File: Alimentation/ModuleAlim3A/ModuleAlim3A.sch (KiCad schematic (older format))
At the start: 18 parts, among them J1 Conn_01x05, J2 Conn_01x02, J3 OUTPUT, U1 PTN78060W_EUW-7, U2 ACS712xLCTR-20A

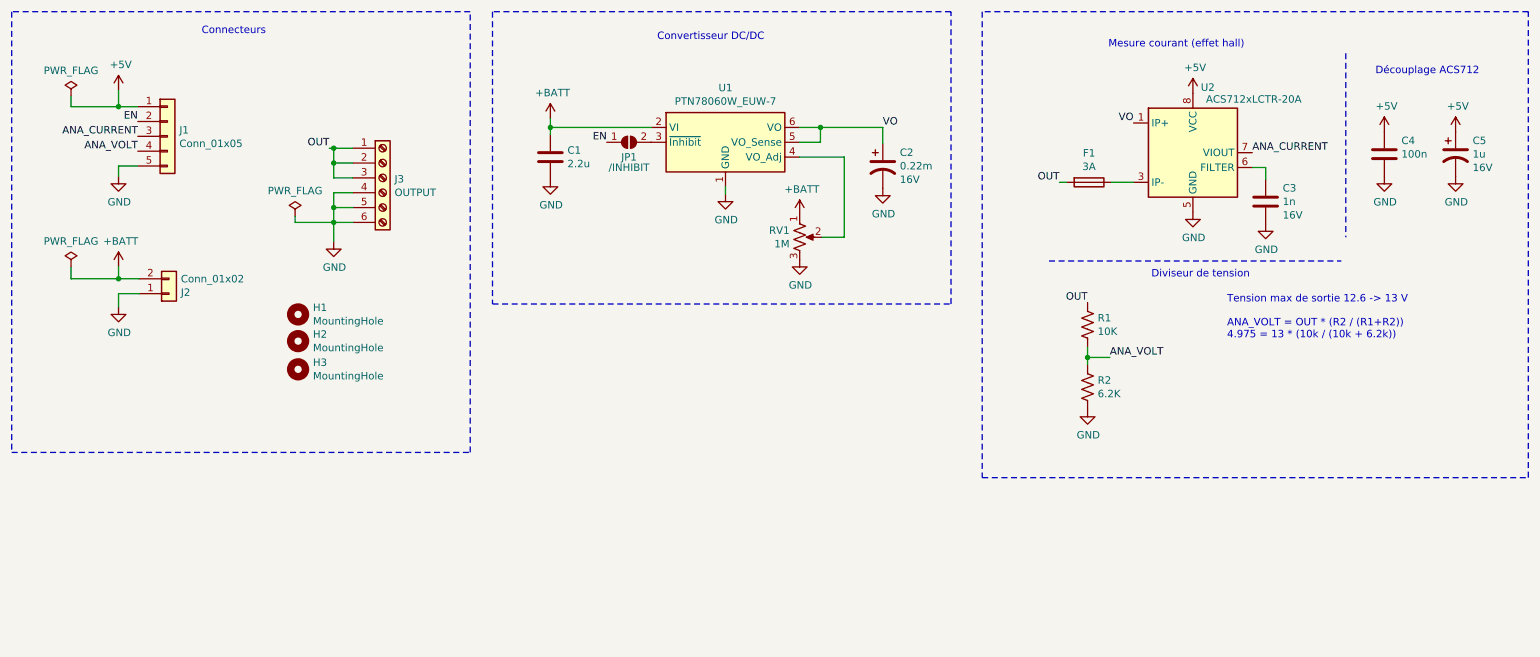
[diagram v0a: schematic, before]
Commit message: Module alim ISO, clean master alim
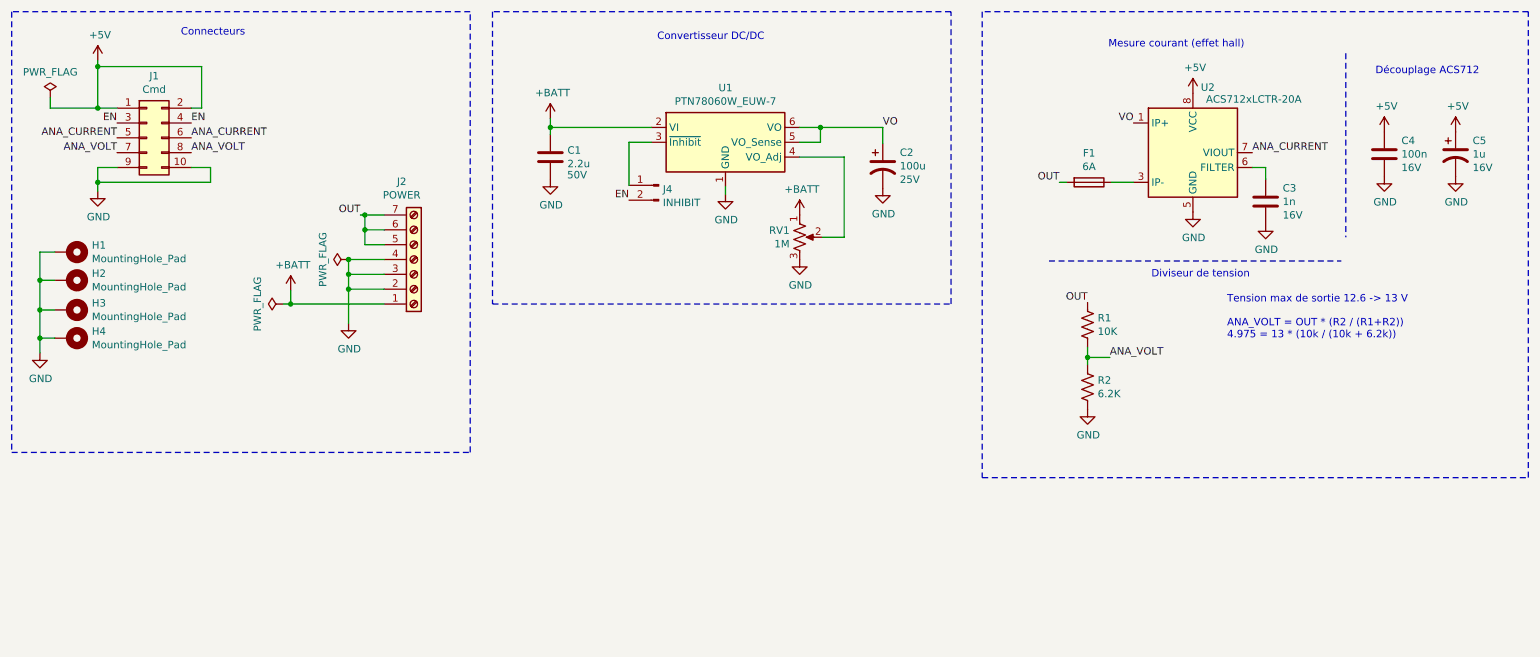
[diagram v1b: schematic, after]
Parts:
- removed H1, H2, H3: MountingHole, MountingHole:MountingHole_3.2mm_M3, symbol Mechanical:MountingHole
- removed J1: Conn_01x05, Connector_JST:JST_PH_B5B-PH-K_1x05_P2.00mm_Vertical, symbol Connector_Generic:Conn_01x05
- removed J2: Conn_01x02, Connector_Phoenix_MC_HighVoltage:PhoenixContact_MC_1,5_2-G-5.08_1x02_P5.08mm_Horizontal, symbol Connector_Generic:Conn_01x02
- removed J3: OUTPUT, TerminalBlock_Phoenix:TerminalBlock_Phoenix_PT-1,5-6-5.0-H_1x06_P5.00mm_Horizontal, symbol Connector:Screw_Terminal_01x06
- removed JP1: /INHIBIT, Jumper:SolderJumper-2_P1.3mm_Open_RoundedPad1.0x1.5mm, symbol Jumper:SolderJumper_2_Open
- added H1, H2, H3, H4: MountingHole_Pad, MountingHole:MountingHole_3.2mm_M3_Pad_Via, symbol Mechanical:MountingHole_Pad
- added J1: Cmd, Connector_IDC:IDC-Header_2x05_P2.54mm_Vertical, symbol Connector_Generic:Conn_02x05_Odd_Even
- added J2: POWER, TerminalBlock_Phoenix:TerminalBlock_Phoenix_MKDS-1,5-7-5.08_1x07_P5.08mm_Horizontal, symbol Connector:Screw_Terminal_01x07
- added J4: INHIBIT, Connector_PinHeader_2.54mm:PinHeader_1x02_P2.54mm_Vertical, symbol Connector:Conn_01x02_Male
- C1: footprint Capacitor_SMD:C_0805_2012Metric_Pad1.18x1.45mm_HandSolder -> Capacitor_SMD:C_1206_3216Metric_Pad1.33x1.80mm_HandSolder; LCSC Part (none) -> C282852; Tension (none) -> 50V
- C2: value 0.22m -> 100u; footprint Capacitor_SMD:CP_Elec_8x6.2 -> Capacitor_SMD:CP_Elec_6.3x7.7; LCSC Part (none) -> C176675; Tension 16V -> 25V
- C3: LCSC Part (none) -> C163169
- C4: footprint Capacitor_SMD:C_0805_2012Metric_Pad1.18x1.45mm_HandSolder -> Capacitor_SMD:C_0603_1608Metric_Pad1.08x0.95mm_HandSolder; LCSC Part (none) -> C80516; Tension (none) -> 16V
- C5: LCSC Part (none) -> C249445
- F1: value 3A -> 6A; JLCPCB BOM (none) -> 0
- R1: LCSC Part (none) -> C191317
- R2: LCSC Part (none) -> C413691
- RV1: footprint Potentiometer_SMD:Potentiometer_Bourns_TC33X_Vertical -> Potentiometer_THT:Potentiometer_Bourns_3266Y_Vertical; JLCPCB BOM (none) -> 0
- U2: LCSC Part (none) -> C10681
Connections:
- net +5V: now also J1.1 (Pin_1), J1.2 (Pin_2)
- net +BATT: now also J2.1 (Pin_1)
- net ANA_CURRENT: now also J1.5 (Pin_5), J1.6 (Pin_6)
- net ANA_VOLT: now also J1.7 (Pin_7), J1.8 (Pin_8)
- net EN: now also J1.3 (Pin_3), J1.4 (Pin_4), J4.2 (Pin_2)
- net GND: now also H1.1, H2.1, H3.1, H4.1, J1.10 (Pin_10), J1.9 (Pin_9), J2.2 (Pin_2), J2.3 (Pin_3), J2.4 (Pin_4)
- net OUT: now also J2.5 (Pin_5), J2.6 (Pin_6), J2.7 (Pin_7)
- net at U1.3 (~Inhibit): now also J4.1 (Pin_1)

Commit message: Modules Alim 3A et 6A uniforme sans mesure courant/tension
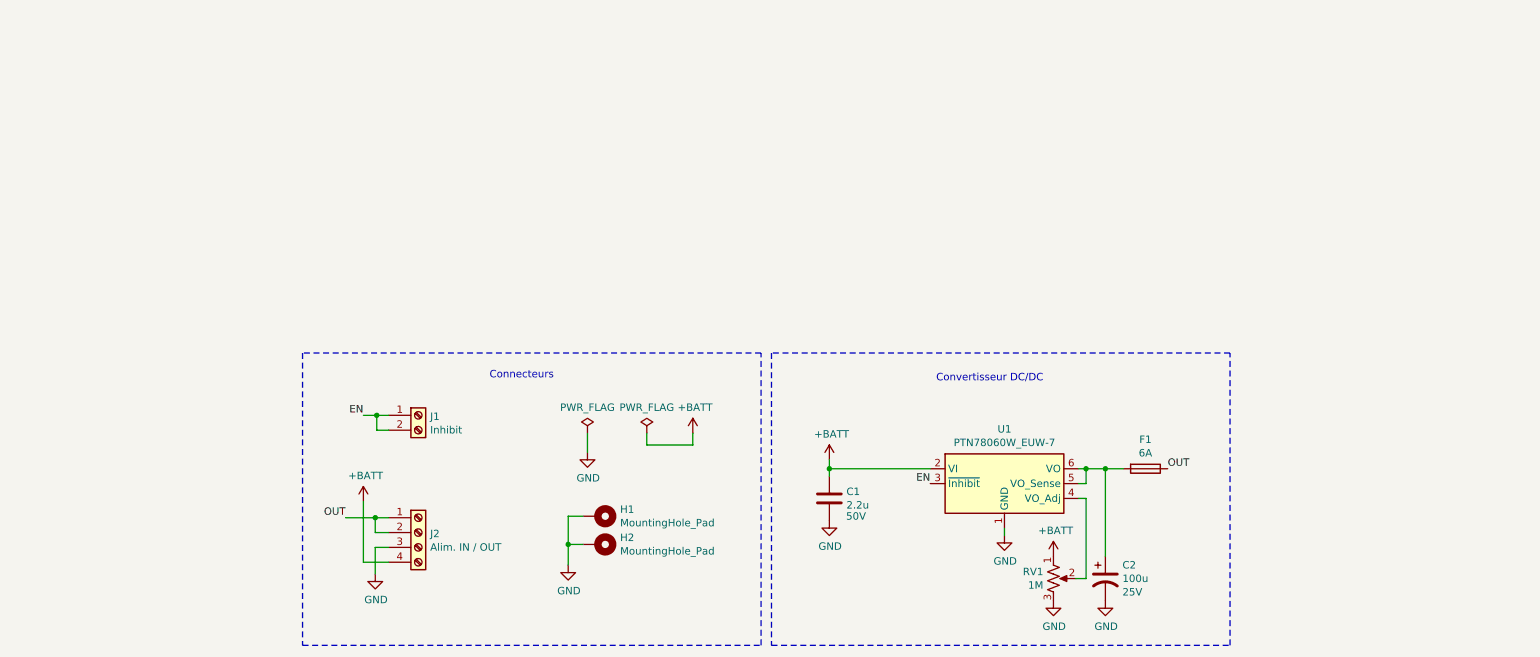
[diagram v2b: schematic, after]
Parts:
- removed C3: 1n, Capacitor_SMD:C_0603_1608Metric_Pad1.08x0.95mm_HandSolder, symbol Device:C
- removed C4: 100n, Capacitor_SMD:C_0603_1608Metric_Pad1.08x0.95mm_HandSolder, symbol Device:C
- removed C5: 1u, Capacitor_SMD:CP_Elec_4x5.3, symbol Device:CP1
- removed H3, H4: MountingHole_Pad, MountingHole:MountingHole_3.2mm_M3_Pad_Via, symbol Mechanical:MountingHole_Pad
- removed J1: Cmd, Connector_IDC:IDC-Header_2x05_P2.54mm_Vertical, symbol Connector_Generic:Conn_02x05_Odd_Even
- removed J2: POWER, TerminalBlock_Phoenix:TerminalBlock_Phoenix_MKDS-1,5-7-5.08_1x07_P5.08mm_Horizontal, symbol Connector:Screw_Terminal_01x07
- removed J4: INHIBIT, Connector_PinHeader_2.54mm:PinHeader_1x02_P2.54mm_Vertical, symbol Connector:Conn_01x02_Male
- removed R1: 10K, Resistor_SMD:R_0805_2012Metric_Pad1.20x1.40mm_HandSolder, symbol Device:R_US
- removed R2: 6.2K, Resistor_SMD:R_0805_2012Metric_Pad1.20x1.40mm_HandSolder, symbol Device:R_US
- removed U2: ACS712xLCTR-20A, Package_SO:SOIC-8_3.9x4.9mm_P1.27mm, symbol Sensor_Current:ACS712xLCTR-20A
- added J1: Inhibit, TerminalBlock_Phoenix:TerminalBlock_Phoenix_MPT-0,5-2-2.54_1x02_P2.54mm_Horizontal, symbol Connector:Screw_Terminal_01x02
- added J2: Alim. IN / OUT, TerminalBlock_Phoenix:TerminalBlock_Phoenix_MKDS-1,5-4-5.08_1x04_P5.08mm_Horizontal, symbol Connector:Screw_Terminal_01x04
- U1: JLCPCB BOM (none) -> 0
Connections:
- net +BATT: now also J2.4 (Pin_4)
- net EN: now also U1.3 (~Inhibit), J1.1 (Pin_1), J1.2 (Pin_2)
- net GND: now also J2.3 (Pin_3)
- net OUT: now also F1.1, J2.1 (Pin_1), J2.2 (Pin_2); no longer F1.2
- net VO: no longer names the net of C2.1, U1.5 (VO_Sense), U1.6 (VO)
- net VO: now also F1.2
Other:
- note removed: "Diviseur de tension"
- note removed: "Découplage ACS712"
- note removed: "Mesure courant (effet hall)"
- note removed: "Tension max de sortie 12.6 -> 13 V\n\nANA_VOLT = OUT * (R2 / (R1+R2))\n4.975 = 13 * (10k / (10k + 6.2k))"
- moved on the sheet: C1, C2, F1, H1, H2, RV1, U1

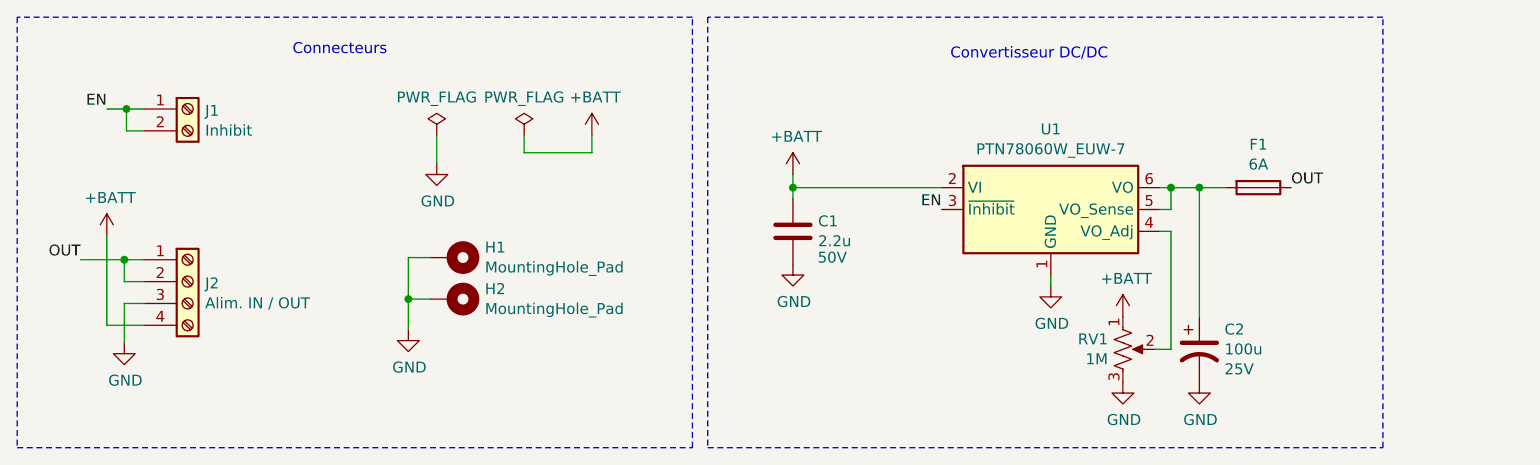
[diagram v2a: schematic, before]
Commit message: Finalisation modules 3A et 6A, routage master alim
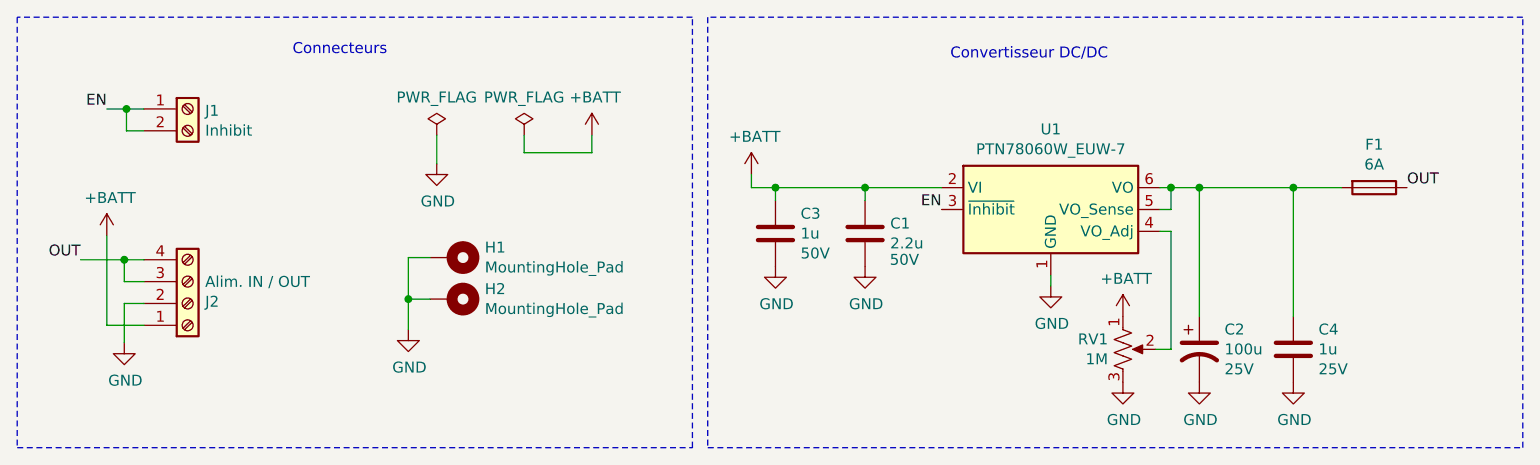
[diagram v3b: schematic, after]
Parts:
- added C3: 1u, Capacitor_SMD:C_0603_1608Metric_Pad1.08x0.95mm_HandSolder, symbol Device:C
- added C4: 1u, Capacitor_SMD:C_0402_1005Metric_Pad0.74x0.62mm_HandSolder, symbol Device:C
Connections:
- net +BATT: now also J2.1 (Pin_1), C3.1; no longer J2.4 (Pin_4)
- net GND: now also J2.2 (Pin_2), C3.2, C4.2; no longer J2.3 (Pin_3)
- net OUT: now also J2.3 (Pin_3), J2.4 (Pin_4); no longer J2.1 (Pin_1), J2.2 (Pin_2)
- net at C2.1, F1.2, U1.5 (VO_Sense)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: now also C4.1
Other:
- moved on the sheet: C1, F1
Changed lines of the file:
@@
 EN
-$Comp
-L power:+BATT #PWR06
-U 1 1 5FC582F6
-P 6180 3710
-F 0 "#PWR06" H 6180 3560 50  0001 C CNN
-F 1 "+BATT" H 6195 3883 50  0000 C CNN
-F 2 "" H 6180 3710 50  0001 C CNN
-F 3 "" H 6180 3710 50  0001 C CNN
-	1    6180 3710
-	1    0    0    -1
-$EndComp
 $Comp
 L power:GND #PWR07
 U 1 1 5FC59EE3
-P 6180 4120
-F 0 "#PWR07" H 6180 3870 50  0001 C CNN
-F 1 "GND" H 6185 3947 50  0000 C CNN
-F 2 "" H 6180 4120 50  0001 C CNN
-F 3 "" H 6180 4120 50  0001 C CNN
-	1    6180 4120
+P 6510 4130
+F 0 "#PWR07" H 6510 3880 50  0001 C CNN
+F 1 "GND" H 6515 3957 50  0000 C CNN
+F 2 "" H 6510 4130 50  0001 C CNN
+F 3 "" H 6510 4130 50  0001 C CNN
+	1    6510 4130
 	1    0    0    -1
 $EndComp
@@
 	1    0    0    -1
 $EndComp
-Wire Wire Line
-	6180 3710 6180 3770
-Wire Wire Line
-	6860 3770 6180 3770
-Connection ~ 6180 3770
-Wire Wire Line
-	6180 3770 6180 3820
 $Comp
 L power:PWR_FLAG #FLG02
@@
 Wire Notes Line
 	2630 2990 2630 4960
-Text Label 8460 3770 0    50   ~ 0
+Text Label 8990 3770 0    50   ~ 0
 OUT
 $Comp
@@
 	5790 2990 5790 4960
 Wire Notes Line
-	5790 4960 8880 4960
-Wire Notes Line
-	8880 4960 8880 2990
-Wire Notes Line
-	8880 2990 5790 2990
+	5790 4960 9520 4960
+Wire Notes Line
+	9520 4960 9520 2990
+Wire Notes Line
+	9520 2990 5790 2990
 Text Notes 6900 3190 0    50   ~ 0
 Convertisseur DC/DC
@@
 L Device:C C1
 U 1 1 5FC576BA
-P 6180 3970
-F 0 "C1" H 6295 4016 50  0000 L CNN
-F 1 "2.2u" H 6295 3925 50  0000 L CNN
-F 2 "Capacitor_SMD:C_1206_3216Metric_Pad1.33x1.80mm_HandSolder" H 6218 3820 50  0001 C CNN
-F 3 "~" H 6180 3970 50  0001 C CNN
-F 4 "50V" H 6360 3850 50  0000 C CNN "Tension"
-F 5 "C282852" H 6180 3970 50  0001 C CNN "LCSC Part"
-	1    6180 3970
+P 6510 3980
+F 0 "C1" H 6625 4026 50  0000 L CNN
+F 1 "2.2u" H 6625 3935 50  0000 L CNN
+F 2 "Capacitor_SMD:C_1206_3216Metric_Pad1.33x1.80mm_HandSolder" H 6548 3830 50  0001 C CNN
+F 3 "~" H 6510 3980 50  0001 C CNN
+F 4 "50V" H 6690 3860 50  0000 C CNN "Tension"
+F 5 "C282852" H 6510 3980 50  0001 C CNN "LCSC Part"
+	1    6510 3980
 	1    0    0    -1
 $EndComp
@@
 L Device:Fuse F1
 U 1 1 5FC87499
-P 8310 3770
-F 0 "F1" V 8113 3770 50  0000 C CNN
-F 1 "6A" V 8204 3770 50  0000 C CNN
-F 2 "Fuse:Fuseholder_Cylinder-5x20mm_Schurter_0031_8201_Horizontal_Open" V 8240 3770 50  0001 C CNN
-F 3 "~" H 8310 3770 50  0001 C CNN
-F 4 "0" H 8310 3770 50  0001 C CNN "JLCPCB BOM"
-	1    8310 3770
+P 8840 3770
+F 0 "F1" V 8643 3770 50  0000 C CNN
+F 1 "6A" V 8734 3770 50  0000 C CNN
+F 2 "Fuse:Fuseholder_Cylinder-5x20mm_Schurter_0031_8201_Horizontal_Open" V 8770 3770 50  0001 C CNN
+F 3 "~" H 8840 3770 50  0001 C CNN
+F 4 "0" H 8840 3770 50  0001 C CNN "JLCPCB BOM"
+	1    8840 3770
 	0    1    1    0
 $EndComp
@@
 	4420 4280 4420 4420
 $Comp
-L Connector:Screw_Terminal_01x04 J2
-U 1 1 5FD55CAF
-P 3410 4200
-F 0 "J2" H 3490 4192 50  0000 L CNN
-F 1 "Alim. IN / OUT" H 3490 4101 50  0000 L CNN
-F 2 "TerminalBlock_Phoenix:TerminalBlock_Phoenix_MKDS-1,5-4-5.08_1x04_P5.08mm_Horizontal" H 3410 4200 50  0001 C CNN
-F 3 "~" H 3410 4200 50  0001 C CNN
-F 4 "0" H 3410 4200 50  0001 C CNN "JLCPCB BOM"
-	1    3410 4200
-	1    0    0    -1
-$EndComp
-$Comp
 L power:+BATT #PWR01
 U 1 1 5FD57137
@@
 	3130 3410 3210 3410
 Wire Wire Line
-	8160 3770 8040 3770
+	8690 3770 8470 3770
 Connection ~ 8040 3770
 Text Notes 3890 3170 0    50   ~ 0
 Connecteurs
+$Comp
+L Connector:Screw_Terminal_01x04 J2
+U 1 1 5FD55CAF
+P 3410 4300
+F 0 "J2" H 3490 4292 50  0000 L CNN
+F 1 "Alim. IN / OUT" H 3490 4201 50  0000 L CNN
+F 2 "TerminalBlock_Phoenix:TerminalBlock_Phoenix_MKDS-1,5-4-5.08_1x04_P5.08mm_Horizontal" H 3410 4300 50  0001 C CNN
+F 3 "~" H 3410 4300 50  0001 C CNN
+F 4 "0" H 3410 4300 50  0001 C CNN "JLCPCB BOM"
+	1    3410 4300
+	1    0    0    1
+$EndComp
+$Comp
+L Device:C C3
+U 1 1 5FEB8135
+P 6100 3980
+F 0 "C3" H 6215 4071 50  0000 L CNN
+F 1 "1u" H 6215 3980 50  0000 L CNN
+F 2 "Capacitor_SMD:C_0603_1608Metric_Pad1.08x0.95mm_HandSolder" H 6138 3830 50  0001 C CNN
+F 3 "~" H 6100 3980 50  0001 C CNN
+F 4 "50V" H 6215 3889 50  0000 L CNN "Tension"
+F 5 "C105174" H 6100 3980 50  0001 C CNN "LCSC Part"
+	1    6100 3980
+	1    0    0    -1
+$EndComp
+$Comp
+L Device:C C4
+U 1 1 5FEBA8A1
+P 8470 4510
+F 0 "C4" H 8585 4601 50  0000 L CNN
+F 1 "1u" H 8585 4510 50  0000 L CNN
+F 2 "Capacitor_SMD:C_0402_1005Metric_Pad0.74x0.62mm_HandSolder" H 8508 4360 50  0001 C CNN
+F 3 "~" H 8470 4510 50  0001 C CNN
+F 4 "25V" H 8585 4419 50  0000 L CNN "Tension"
+F 5 "C52923" H 8470 4510 50  0001 C CNN "LCSC Part"
+	1    8470 4510
+	1    0    0    -1
+$EndComp
+$Comp
+L power:+BATT #PWR06
+U 1 1 5FC582F6
+P 5990 3710
+F 0 "#PWR06" H 5990 3560 50  0001 C CNN
+F 1 "+BATT" H 6005 3883 50  0000 C CNN
+F 2 "" H 5990 3710 50  0001 C CNN
+F 3 "" H 5990 3710 50  0001 C CNN
+	1    5990 3710
+	1    0    0    -1
+$EndComp
+Wire Wire Line
+	6860 3770 6510 3770
+Wire Wire Line
+	5990 3770 5990 3710
+Connection ~ 6100 3770
+Wire Wire Line
+	6100 3770 5990 3770
+Wire Wire Line
+	6510 3830 6510 3770
+Connection ~ 6510 3770
+Wire Wire Line
+	6510 3770 6100 3770
+$Comp
+L power:GND #PWR04
+U 1 1 5FED8191
+P 6100 4130
+F 0 "#PWR04" H 6100 3880 50  0001 C CNN
+F 1 "GND" H 6105 3957 50  0000 C CNN
+F 2 "" H 6100 4130 50  0001 C CNN
+F 3 "" H 6100 4130 50  0001 C CNN
+	1    6100 4130
+	1    0    0    -1
+$EndComp
+Wire Wire Line
+	6100 3770 6100 3830
+Connection ~ 8470 3770
+Wire Wire Line
+	8470 3770 8040 3770
+Wire Wire Line
+	8470 3770 8470 4360
+$Comp
+L power:GND #PWR012
+U 1 1 5FEDAD42
+P 8470 4660
+F 0 "#PWR012" H 8470 4410 50  0001 C CNN
+F 1 "GND" H 8475 4487 50  0000 C CNN
+F 2 "" H 8470 4660 50  0001 C CNN
+F 3 "" H 8470 4660 50  0001 C CNN
+	1    8470 4660
+	1    0    0    -1
+$EndComp
 $EndSCHEMATC

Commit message: Finalisation pour commande pack Alimentation 14/02/2021
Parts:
- C1: LCSC Part C282852 -> C50254
- C3: footprint Capacitor_SMD:C_0603_1608Metric_Pad1.08x0.95mm_HandSolder -> Capacitor_SMD:C_0805_2012Metric_Pad1.18x1.45mm_HandSolder; LCSC Part C105174 -> C28323
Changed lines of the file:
@@
 F 3 "~" H 6510 3980 50  0001 C CNN
 F 4 "50V" H 6690 3860 50  0000 C CNN "Tension"
-F 5 "C282852" H 6510 3980 50  0001 C CNN "LCSC Part"
+F 5 "C50254" H 6510 3980 50  0001 C CNN "LCSC Part"
 	1    6510 3980
 	1    0    0    -1
@@
 F 0 "C3" H 6215 4071 50  0000 L CNN
 F 1 "1u" H 6215 3980 50  0000 L CNN
-F 2 "Capacitor_SMD:C_0603_1608Metric_Pad1.08x0.95mm_HandSolder" H 6138 3830 50  0001 C CNN
+F 2 "Capacitor_SMD:C_0805_2012Metric_Pad1.18x1.45mm_HandSolder" H 6138 3830 50  0001 C CNN
 F 3 "~" H 6100 3980 50  0001 C CNN
 F 4 "50V" H 6215 3889 50  0000 L CNN "Tension"
-F 5 "C105174" H 6100 3980 50  0001 C CNN "LCSC Part"
+F 5 "C28323" H 6100 3980 50  0001 C CNN "LCSC Part"
 	1    6100 3980
 	1    0    0    -1

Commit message: Potar THT module 3A
# Liste des mots clés de titre de commit (version courte -> résultat long)
# r <num> -> Récupération du Redmine (Redmine #<num> : <titre_du_redmine>)
# t <titre> -> Technique : <titre>
# f <titre> -> Fix : <titre>
# ty <titre> -> Typo : <titre>
# d <titre> -> Doc : <titre>
# s <titre> -> Sécurité : <titre>
# u <titre> -> UI : <titre>
# c <titre> -> CI : <titre>
# WIP <desc>
# [skip ci] en début de titre de commit permet de ne pas déclencher de build
#
# Chaque ligne de description ajouté sera préfixé automatiquement d'une puce.
#
# Pour la saisie de temps automatique lors de l'écriture d'un commit le format est le suivant :
# /spend <options>
#
# NB : Plusieurs /spend peuvent être défini sur un même commit
#
# Les options sont :
# - Temps en heure (ie 0.25). Obligatoire
# - Numéro de redmine. Facultatif si le commit porte sur un redmine avec la syntaxe courte ou longue.
# - Catégorie de l'imputation. Facultatif. Récupération par les premières lettres en format court, si non défini Développement sera utilisé
# - Date de l'imputation au format ISO8601 (ie 2021-02-23)
#
# NB : L'imputation n'est pas bloquante pour le message de commit si une erreur survient.
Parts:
- RV1: footprint Potentiometer_THT:Potentiometer_Bourns_3266Y_Vertical -> Potentiometer_THT:Potentiometer_Bourns_3296W_Vertical
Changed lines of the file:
@@
 F 0 "RV1" H 7622 4556 50  0000 R CNN
 F 1 "1M" H 7622 4465 50  0000 R CNN
-F 2 "Potentiometer_THT:Potentiometer_Bourns_3266Y_Vertical" H 7690 4510 50  0001 C CNN
+F 2 "Potentiometer_THT:Potentiometer_Bourns_3296W_Vertical" H 7690 4510 50  0001 C CNN
 F 3 "~" H 7690 4510 50  0001 C CNN
 F 4 "0" H 7690 4510 50  0001 C CNN "JLCPCB BOM"
